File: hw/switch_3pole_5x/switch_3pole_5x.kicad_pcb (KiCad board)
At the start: 2 copper layers, 93 x 67 mm, 72 parts, among them J1 WAGO 2081-1123, J12 CONN-ISP-6, J13 WAGO 243-723, J14 WAGO 243-724, J15 WAGO 243-721, J16 WAGO 243-722, J2 WAGO 2081-1123, J3 WAGO 2081-1123, J4 WAGO 2081-1123, J5 WAGO 2081-1123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

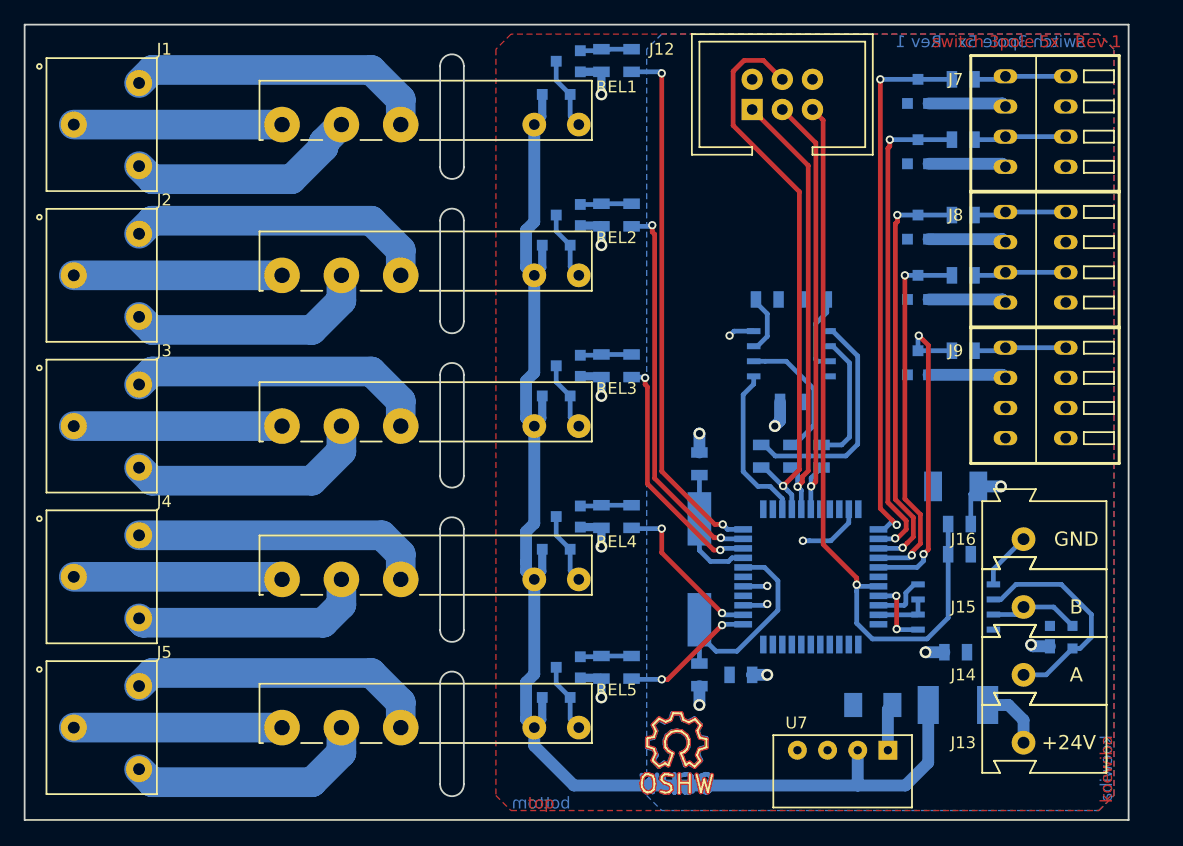
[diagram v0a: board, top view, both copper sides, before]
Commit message: Moved connectors towards inner board to avoid TH pads touching housing
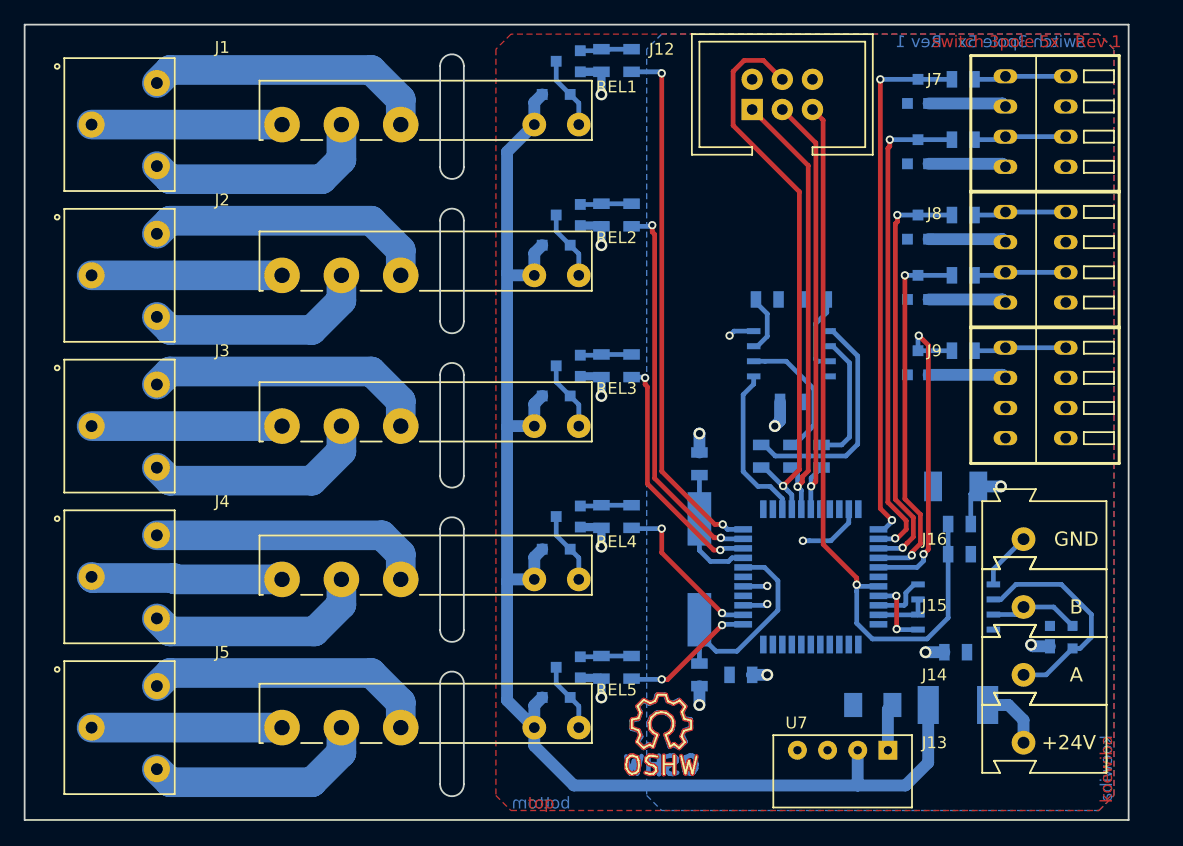
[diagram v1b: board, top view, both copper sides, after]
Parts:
- moved LOGO1 2.04 mm to (153.6, 108.9)
- moved LOGO2 2.04 mm to (153.6, 108.9)
- moved LOGO4 2.04 mm to (153.6, 108.9)
- moved J1 1.50 mm to (111.1, 54.9)
- moved J2 1.50 mm to (111.1, 67.6)
- moved J3 1.50 mm to (111.1, 80.3)
- moved J4 1.50 mm to (111.1, 93.0)
- moved J5 1.50 mm to (111.1, 105.7)
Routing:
- net +24V: track 111.9 -> 118.6 mm
- net /Relays/RELAY_4_NO: track 17.5 -> 16.0 mm
- net /Relays/RELAY_4_NC: track 25.6 -> 24.1 mm
- net /Relays/RELAY_4_COM: track 20.6 -> 19.1 mm
- net /Relays/RELAY_3_NC: track 24.8 -> 23.3 mm
- net /Relays/RELAY_2_NO: track 17.5 -> 16.0 mm
- net /Relays/RELAY_2_NC: track 25.6 -> 24.1 mm
- net /Relays/RELAY_2_COM: track 20.6 -> 19.1 mm
- net /Relays/RELAY_1_NO: track 17.5 -> 16.0 mm
- net /Relays/RELAY_1_NC: track 25.6 -> 24.1 mm
- net /Relays/RELAY_1_COM: track 20.6 -> 19.1 mm
- net /Relays/RELAY_0_NO: track 17.5 -> 16.0 mm
- net /Relays/RELAY_0_NC: track 25.6 -> 24.1 mm
- net /Relays/RELAY_3_NO: track 17.6 -> 16.4 mm
- net //button_0: track 46.1 -> 45.1 mm
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
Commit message: added testpoints and LEDs updated 3d footprints
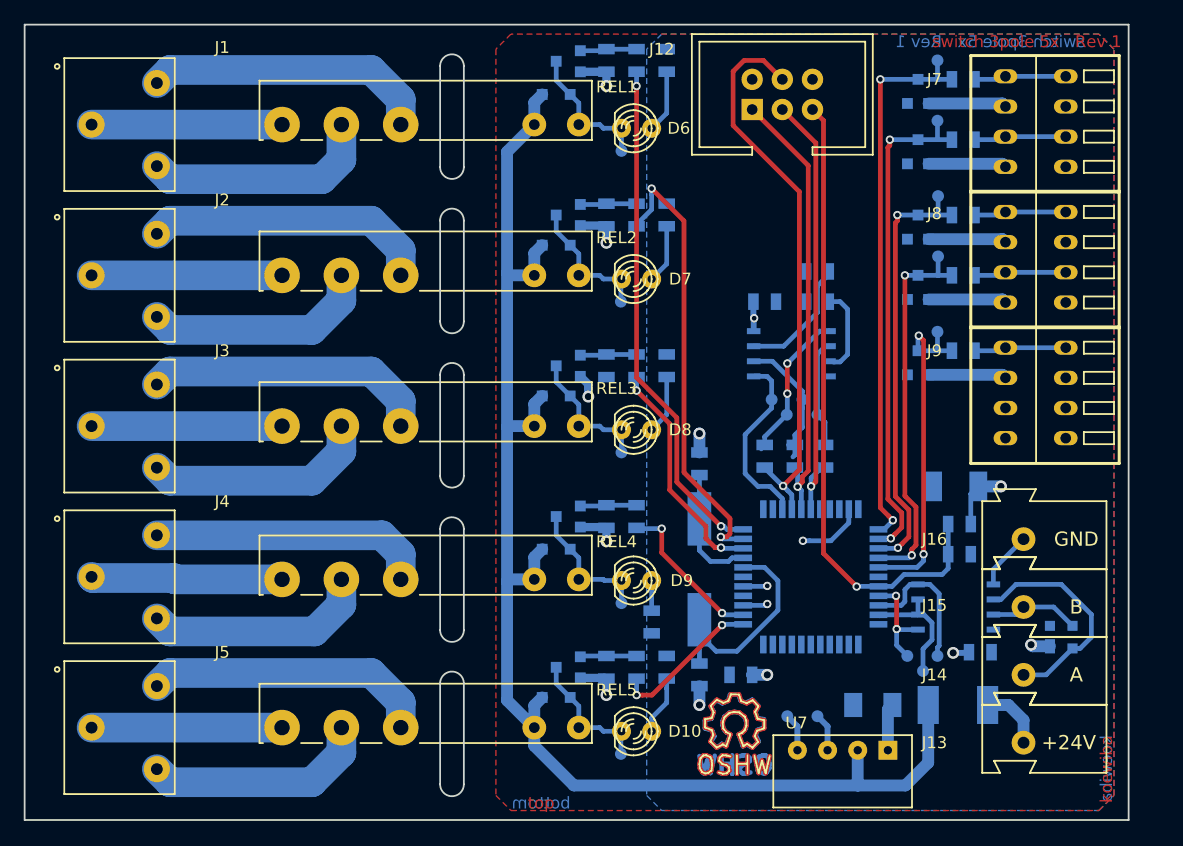
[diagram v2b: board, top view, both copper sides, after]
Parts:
- added D10: green, 2,2V/2mA, LED:LED_RM2.54mm_D3mm, F.Cu at (151.6, 109.5)
- added D6: green, 2,2V/2mA, LED:LED_RM2.54mm_D3mm, F.Cu at (151.6, 58.7)
- added D7: green, 2,2V/2mA, LED:LED_RM2.54mm_D3mm, F.Cu at (151.6, 71.4)
- added D8: green, 2,2V/2mA, LED:LED_RM2.54mm_D3mm, F.Cu at (151.6, 84.1)
- added D9: green, 2,2V/2mA, LED:LED_RM2.54mm_D3mm, F.Cu at (151.6, 96.8)
- added J10: tp_relay_1, Connector_Miscelleaneus:Testpoint_1mm, B.Cu at (150.3, 73.3)
- added J11: tp_relay_2, Connector_Miscelleaneus:Testpoint_1mm, B.Cu at (150.3, 86.0)
- added J17: tp_relay_3, Connector_Miscelleaneus:Testpoint_1mm, B.Cu at (150.3, 98.7)
- added J18: tp_relay_4, Connector_Miscelleaneus:Testpoint_1mm, B.Cu at (150.3, 111.4)
- added J19: tp_button_0, Connector_Miscelleaneus:Testpoint_1mm, B.Cu at (176.9, 53.0)
- added J20: tp_button_1, Connector_Miscelleaneus:Testpoint_1mm, B.Cu at (176.9, 58.1)
- added J21: tp_button_2, Connector_Miscelleaneus:Testpoint_1mm, B.Cu at (177.0, 64.4)
- added J22: tp_button_3, Connector_Miscelleaneus:Testpoint_1mm, B.Cu at (177.0, 69.5)
- added J23: tp_button_4, Connector_Miscelleaneus:Testpoint_1mm, B.Cu at (176.9, 75.9)
- added J24: tp_cseep, Connector_Miscelleaneus:Testpoint_1mm, B.Cu at (163.0, 81.6)
- added J25: tp_miso, Connector_Miscelleaneus:Testpoint_1mm, B.Cu at (165.6, 81.6)
- added J26: tp_mosi, Connector_Miscelleaneus:Testpoint_1mm, B.Cu at (164.2, 82.9)
- added J27: tp_sck, Connector_Miscelleaneus:Testpoint_1mm, B.Cu at (166.8, 82.9)
- added J28: tp_txden, Connector_Miscelleaneus:Testpoint_1mm, B.Cu at (175.7, 104.5)
- added J29: tp_txd, Connector_Miscelleaneus:Testpoint_1mm, B.Cu at (176.9, 103.2)
- added J30: tp_rxd, Connector_Miscelleaneus:Testpoint_1mm, B.Cu at (174.4, 103.2)
- added J31: tp_vcc, Connector_Miscelleaneus:Testpoint_1mm, B.Cu at (164.3, 108.3)
- added J32: tp_gnd, Connector_Miscelleaneus:Testpoint_1mm, B.Cu at (166.8, 108.3)
- added J6: tp_relay_0, Connector_Miscelleaneus:Testpoint_1mm, B.Cu at (150.3, 60.6)
- added R12: 1k5, Resistor:R_0805, B.Cu at (154.1, 66.0)
- added R13: 1k5, Resistor:R_0805, B.Cu at (154.1, 78.7)
- added R14: 1k5, Resistor:R_0805, B.Cu at (152.8, 100.3)
- added R15: 1k5, Resistor:R_0805, B.Cu at (154.1, 104.1)
- added R6: 1k5, Resistor:R_0805, B.Cu at (154.1, 53.0)
- moved C4 8.75 mm to (162.3, 73.3)
- moved LOGO1 6.17 mm to (159.8, 108.9)
- moved LOGO2 6.17 mm to (159.8, 108.9)
- moved LOGO4 6.17 mm to (159.8, 108.9)
- moved R31 4.84 mm to (166.8, 70.8), turned to 0 degrees
- moved C9 2.07 mm to (180.5, 102.9)
- moved R7 0.42 mm to (151.6, 53.0)
- moved R1 0.42 mm to (149.0, 53.0)
- moved R10 0.42 mm to (151.6, 91.4)
- moved R11 0.42 mm to (151.6, 104.1)
- moved R8 0.42 mm to (151.6, 66.0)
- moved R9 0.42 mm to (151.6, 78.7)
- moved R2 0.42 mm to (149.0, 66.0)
- moved R3 0.42 mm to (149.0, 78.7)
- moved R4 0.42 mm to (149.0, 91.4)
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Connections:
- R3 pad 2: GND -> (no net)
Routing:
- net /bus_atmega328_basic//RESET: track 63.6 -> 53.8 mm
- net /bus_atmega328_basic/TXD0: track 4.60 -> 12.1 mm
- net /bus_atmega328_basic/MOSI: track 19.6 -> 13.0 mm, vias 0 -> 2
- net /relay_1: track 32.8 -> 38.7 mm
- net /bus_atmega328_basic/TXD0EN: track 4.73 -> 10.6 mm
- net Net-(R31-Pad2): track 4.99 -> 10.7 mm
- net Net-(D10-Pad2): track 5.87 -> 11.5 mm
- net Net-(D2-Pad1): track 5.87 -> 11.5 mm
- net Net-(D3-Pad1): track 5.87 -> 11.5 mm
- net Net-(D1-Pad1): track 6.12 -> 11.8 mm
- net Net-(D4-Pad1): track 6.08 -> 11.6 mm
- net Net-(D6-Pad1): track 0.00 -> 5.29 mm
- net Net-(D10-Pad1): track 0.00 -> 4.97 mm
- net Net-(D7-Pad1): track 0.00 -> 4.97 mm
- net Net-(D8-Pad1): track 0.00 -> 4.97 mm
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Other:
- net class Power: trace_width 1 -> 0.5
